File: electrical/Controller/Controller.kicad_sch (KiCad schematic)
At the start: 49 parts, among them J1 USB4105-GF-A, J2 UART, J3 SWD, J4 TC2030-NL, J5 I2C, SW1 SYS, U1 USBLC6-2P6, U2 LP5912-3.3DRV, U3 W25Q16JVUXIQ, U4 RP2040, U5 ABPMRRV060MG2A3, Y1 ABM8-272-T3

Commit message: Rename symbol library
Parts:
- H2: symbol midi_concertina:LightPipe -> MidiConcertina:LightPipe
- U5: symbol midi_concertina:ABPMRRV060MG2A3 -> MidiConcertina:ABPMRRV060MG2A3
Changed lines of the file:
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@@
 	)
 	(symbol
-		(lib_id "midi_concertina:ABPMRRV060MG2A3")
+		(lib_id "MidiConcertina:ABPMRRV060MG2A3")
 		(at 356.87 130.81 0)
 		(unit 1)
@@
 	)
 	(symbol
-		(lib_id "midi_concertina:LightPipe")
+		(lib_id "MidiConcertina:LightPipe")
 		(at 374.65 212.09 0)
 		(unit 1)

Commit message: Rename footprint library
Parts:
- H2: footprint midi_concertina:SLP3-150-150-F -> MidiConcertina:Bivar_SLP3-150-150-F
- U5: footprint midi_concertina:Honeywell_ABPMRRx -> MidiConcertina:Honeywell_ABPMRRx
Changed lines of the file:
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@@
 			)
 		)
-		(property "Footprint" "midi_concertina:Honeywell_ABPMRRx"
+		(property "Footprint" "MidiConcertina:Honeywell_ABPMRRx"
 			(at 356.87 130.81 0)
 			(effects
@@
 			)
 		)
-		(property "Footprint" "midi_concertina:SLP3-150-150-F"
+		(property "Footprint" "MidiConcertina:Bivar_SLP3-150-150-F"
 			(at 374.65 212.09 0)
 			(effects

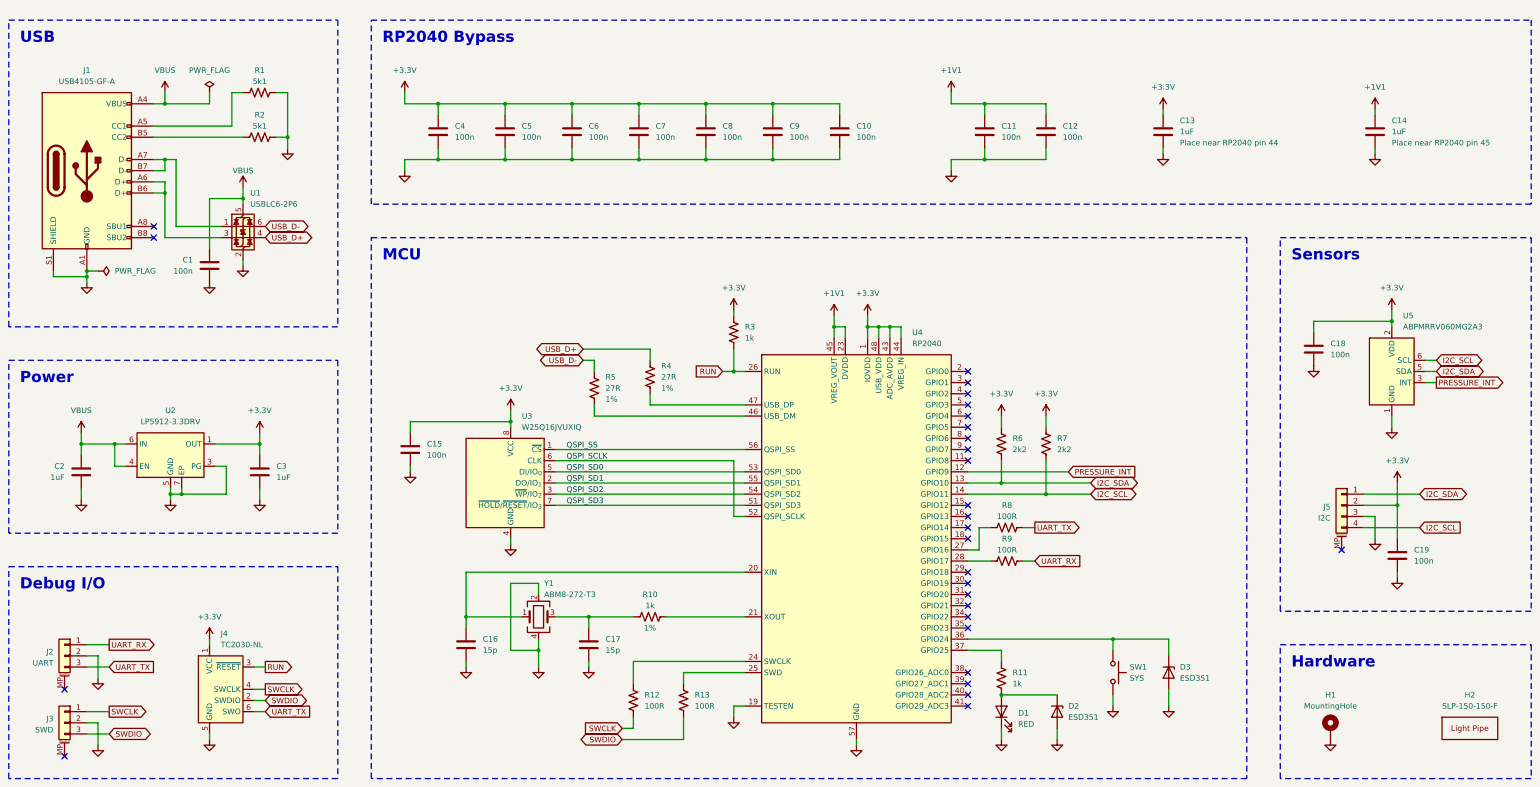
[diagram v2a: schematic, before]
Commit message: Replace pressure sensor with correct part and fatten power traces
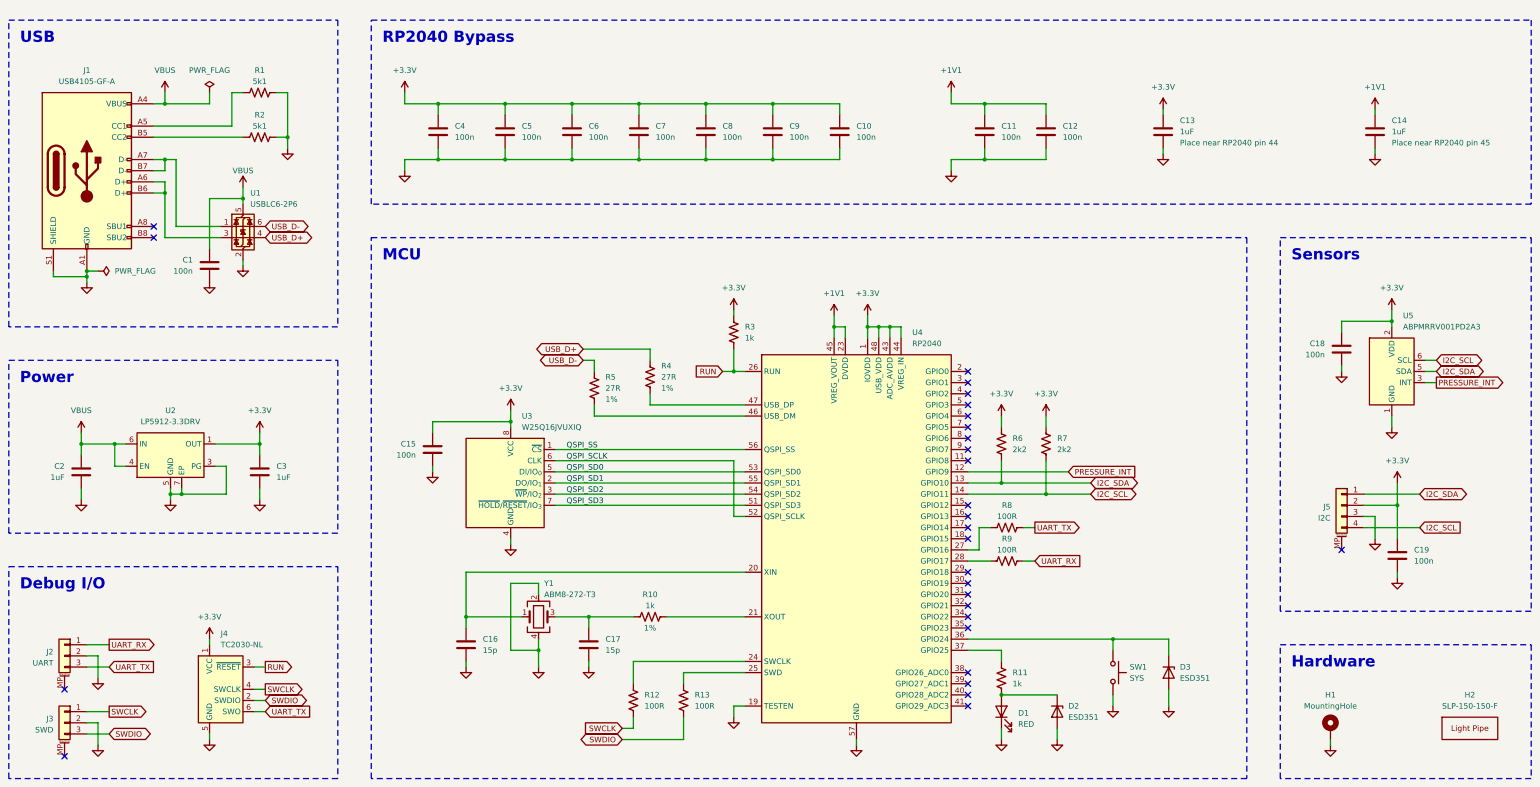
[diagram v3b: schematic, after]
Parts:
- U5: value ABPMRRV060MG2A3 -> ABPMRRV001PD2A3; symbol MidiConcertina:ABPMRRV060MG2A3 -> MidiConcertina:Honeywell_ABPx2x; LCSC C22270183 -> (none)
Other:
- moved on the sheet: C15, C18
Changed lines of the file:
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@@
 	(wire
 		(pts
-			(xy 133.35 153.67) (xy 133.35 152.4)
+			(xy 138.43 153.67) (xy 138.43 152.4)
 		)
 		(stroke
@@
 	(wire
 		(pts
-			(xy 133.35 142.24) (xy 156.21 142.24)
+			(xy 138.43 142.24) (xy 156.21 142.24)
 		)
 		(stroke
@@
 	(wire
 		(pts
-			(xy 339.09 119.38) (xy 356.87 119.38)
+			(xy 345.44 119.38) (xy 356.87 119.38)
 		)
 		(stroke
@@
 	(wire
 		(pts
+			(xy 345.44 130.81) (xy 345.44 129.54)
+		)
+		(stroke
+			(width 0)
+			(type default)
+		)
+	)
+	(wire
+		(pts
 			(xy 132.08 67.31) (xy 132.08 69.85)
 		)
@@
 	(wire
 		(pts
-			(xy 339.09 121.92) (xy 339.09 119.38)
+			(xy 345.44 121.92) (xy 345.44 119.38)
 		)
 		(stroke
@@
 	(wire
 		(pts
-			(xy 133.35 144.78) (xy 133.35 142.24)
+			(xy 138.43 144.78) (xy 138.43 142.24)
 		)
 		(stroke
@@
 	(wire
 		(pts
+			(xy 342.9 215.9) (xy 342.9 214.63)
+		)
+		(stroke
+			(width 0)
+			(type default)
+		)
+	)
+	(wire
+		(pts
 			(xy 181.61 214.63) (xy 195.58 214.63)
 		)
@@
 	(symbol
 		(lib_id "power:GND")
-		(at 339.09 129.54 0)
+		(at 345.44 130.81 0)
 		(unit 1)
 		(exclude_from_sim no)
@@
 		(fields_autoplaced yes)
 		(property "Reference" "#PWR0111"
-			(at 339.09 135.89 0)
+			(at 345.44 137.16 0)
 			(effects
 				(font
@@
 		)
 		(property "Value" "GND"
-			(at 339.09 134.62 0)
+			(at 345.44 135.89 0)
 			(effects
 				(font
@@
 		)
 		(property "Footprint" ""
-			(at 339.09 129.54 0)
+			(at 345.44 130.81 0)
 			(effects
 				(font
@@
 		)
 		(property "Datasheet" ""
-			(at 339.09 129.54 0)
+			(at 345.44 130.81 0)
 			(effects
 				(font
@@
 		)
 		(property "Description" "Power symbol creates a global label with name \"GND\" , ground"
-			(at 339.09 129.54 0)
+			(at 345.44 130.81 0)
 			(effects
 				(font
@@
 	(symbol
 		(lib_id "power:GND")
-		(at 133.35 153.67 0)
+		(at 138.43 153.67 0)
 		(unit 1)
 		(exclude_from_sim no)
@@
 		(fields_autoplaced yes)
 		(property "Reference" "#PWR0120"
-			(at 133.35 160.02 0)
+			(at 138.43 160.02 0)
 			(effects
 				(font
@@
 		)
 		(property "Value" "GND"
-			(at 133.35 158.75 0)
+			(at 138.43 158.75 0)
 			(effects
 				(font
@@
 		)
 		(property "Footprint" ""
-			(at 133.35 153.67 0)
+			(at 138.43 153.67 0)
 			(effects
 				(font
@@
 		)
 		(property "Datasheet" ""
-			(at 133.35 153.67 0)
+			(at 138.43 153.67 0)
 			(effects
 				(font
@@
 		)
 		(property "Description" "Power symbol creates a global label with name \"GND\" , ground"
-			(at 133.35 153.67 0)
+			(at 138.43 153.67 0)
 			(effects
 				(font
@@
 	(symbol
 		(lib_id "Device:C")
-		(at 133.35 148.59 0)
+		(at 138.43 148.59 0)
+		(mirror y)
 		(unit 1)
 		(exclude_from_sim no)
@@
 		(dnp no)
 		(property "Reference" "C15"
-			(at 137.16 147.3199 0)
+			(at 134.62 147.3199 0)
 			(effects
 				(font
@@
 		)
 		(property "Value" "100n"
-			(at 137.16 149.8599 0)
+			(at 134.62 149.8599 0)
 			(effects
 				(font
@@
 		)
 		(property "Footprint" "Capacitor_SMD:C_0402_1005Metric"
-			(at 134.3152 152.4 0)
+			(at 137.4648 152.4 0)
 			(effects
 				(font
@@
 		)
 		(property "Datasheet" "~"
-			(at 133.35 148.59 0)
+			(at 138.43 148.59 0)
 			(effects
 				(font
@@
 		)
 		(property "Description" "Unpolarized capacitor"
-			(at 133.35 148.59 0)
+			(at 138.43 148.59 0)
 			(effects
 				(font
@@
 		)
 		(property "LCSC" "C1525"
-			(at 133.35 148.59 0)
+			(at 138.43 148.59 0)
 			(effects
 				(font
@@
 	(symbol
 		(lib_id "Device:C")
-		(at 339.09 125.73 0)
+		(at 345.44 125.73 0)
+		(mirror y)
 		(unit 1)
 		(exclude_from_sim no)
@@
 		(on_board yes)
 		(dnp no)
-		(fields_autoplaced yes)
 		(property "Reference" "C18"
-			(at 342.9 124.4599 0)
+			(at 341.63 124.4599 0)
 			(effects
 				(font
@@
 		)
 		(property "Value" "100n"
-			(at 342.9 126.9999 0)
+			(at 341.63 126.9999 0)
 			(effects
 				(font
@@
 		)
 		(property "Footprint" "Capacitor_SMD:C_0402_1005Metric"
-			(at 340.0552 129.54 0)
+			(at 344.4748 129.54 0)
 			(effects
 				(font
@@
 		)
 		(property "Datasheet" "~"
-			(at 339.09 125.73 0)
+			(at 345.44 125.73 0)
 			(effects
 				(font
@@
 		)
 		(property "Description" "Unpolarized capacitor"
-			(at 339.09 125.73 0)
+			(at 345.44 125.73 0)
 			(effects
 				(font
@@
 		)
 		(property "LCSC" "C1525"
-			(at 339.09 125.73 0)
+			(at 345.44 125.73 0)
 			(effects
 				(font
@@
 	(symbol
 		(lib_id "power:GND")
-		(at 342.9 214.63 0)
+		(at 342.9 215.9 0)
 		(unit 1)
 		(exclude_from_sim no)
@@
 		(fields_autoplaced yes)
 		(property "Reference" "#PWR0140"
-			(at 342.9 220.98 0)
+			(at 342.9 222.25 0)
 			(effects
 				(font
@@
 		)
 		(property "Value" "GND"
-			(at 342.9 219.71 0)
+			(at 342.9 220.98 0)
 			(effects
 				(font
@@
 		)
 		(property "Footprint" ""
-			(at 342.9 214.63 0)
+			(at 342.9 215.9 0)
 			(effects
 				(font
@@
 		)
 		(property "Datasheet" ""
-			(at 342.9 214.63 0)
+			(at 342.9 215.9 0)
 			(effects
 				(font
@@
 		)
 		(property "Description" "Power symbol creates a global label with name \"GND\" , ground"
-			(at 342.9 214.63 0)
+			(at 342.9 215.9 0)
 			(effects
 				(font
@@
 	)
 	(symbol
-		(lib_id "MidiConcertina:ABPMRRV060MG2A3")
+		(lib_id "MidiConcertina:Honeywell_ABPx2x")
 		(at 356.87 130.81 0)
 		(unit 1)
@@
 			)
 		)
-		(property "Value" "ABPMRRV060MG2A3"
+		(property "Value" "ABPMRRV001PD2A3"
 			(at 359.41 120.65 0)
 			(effects
@@
 			)
 		)
-		(property "LCSC" "C22270183"
+		(property "LCSC" ""
 			(at 356.87 130.81 0)
 			(effects
